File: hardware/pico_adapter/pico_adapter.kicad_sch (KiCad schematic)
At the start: 43 parts, among them J1 L77HDE15SD1CH4F, J2 AudioJack3, J3 5V in, Q1 Q_NMOS_DGS, Q2 Q_NMOS_DGS

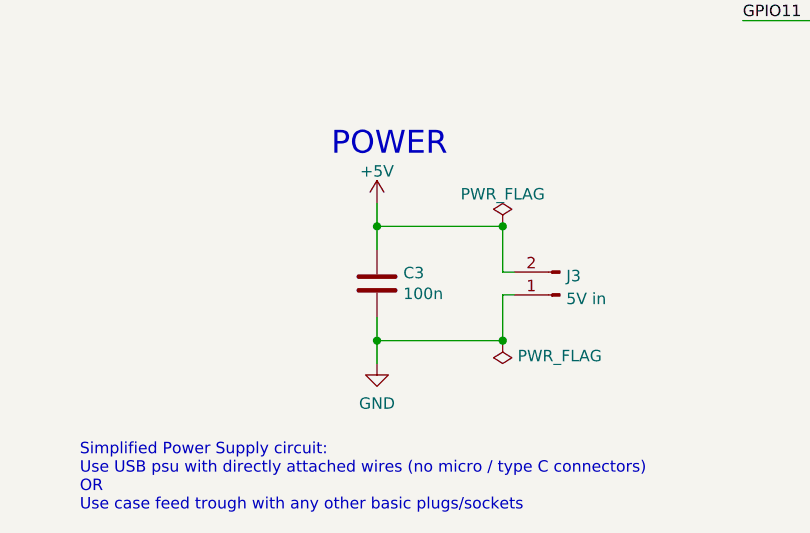
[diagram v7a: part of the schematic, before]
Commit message: UPDATED PICO FOOTPRINT [!] + smaller board
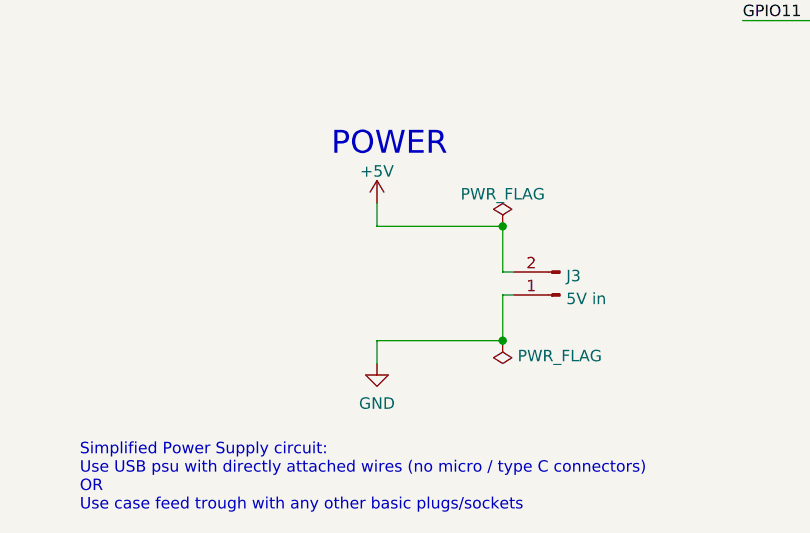
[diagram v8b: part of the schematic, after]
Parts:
- removed C3: 100n, Capacitor_THT:C_Rect_L7.5mm_W6.5mm_P5.00mm, symbol Device:C
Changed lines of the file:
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@@
   (junction (at 137.16 35.56) (diameter 0) (color 0 0 0 0)
   )
-  (junction (at 66.04 138.43) (diameter 0) (color 0 0 0 0)
-  )
   (junction (at 137.16 30.48) (diameter 0) (color 0 0 0 0)
   )
   (junction (at 123.19 62.23) (diameter 0) (color 0 0 0 0)
-  )
-  (junction (at 66.04 151.13) (diameter 0) (color 0 0 0 0)
   )
   (junction (at 220.98 40.64) (diameter 0) (color 0 0 0 0)
@@
     (stroke (width 0) (type default) (color 0 0 0 0))
   )
-  (wire (pts (xy 66.04 138.43) (xy 66.04 140.97))
-    (stroke (width 0) (type default) (color 0 0 0 0))
-  )
   (wire (pts (xy 123.19 25.4) (xy 127 25.4))
     (stroke (width 0) (type default) (color 0 0 0 0))
@@
   )
   (wire (pts (xy 26.67 46.99) (xy 43.18 46.99))
-    (stroke (width 0) (type default) (color 0 0 0 0))
-  )
-  (wire (pts (xy 66.04 148.59) (xy 66.04 151.13))
     (stroke (width 0) (type default) (color 0 0 0 0))
   )
@@
     (pin "9")
   )
-  (symbol (lib_id "Device:C") (at 66.04 144.78 0) (unit 1)
-    (in_bom yes) (on_board yes)
-    (property "Reference" "C3" (id 0) (at 68.961 143.6116 0)
-      (effects (font (size 1.27 1.27)) (justify left))
-    )
-    (property "Value" "100n" (id 1) (at 68.961 145.923 0)
-      (effects (font (size 1.27 1.27)) (justify left))
-    )
-    (property "Footprint" "Capacitor_THT:C_Rect_L7.5mm_W6.5mm_P5.00mm" (id 2) (at 67.0052 148.59 0)
-      (effects (font (size 1.27 1.27)) hide)
-    )
-    (property "Datasheet" "~" (id 3) (at 66.04 144.78 0)
-      (effects (font (size 1.27 1.27)) hide)
-    )
-    (pin "1")
-    (pin "2")
-  )
   (symbol (lib_id "power:PWR_FLAG") (at 80.01 138.43 0) (unit 1)
     (in_bom yes) (on_board yes) (fields_autoplaced)
@@
       (reference "C2") (unit 1) (value "100n") (footprint "Capacitor_THT:C_Rect_L7.5mm_W6.5mm_P5.00mm")
     )
-    (path "/0f4acae6-1474-4661-9a34-e961377aaac1"
-      (reference "C3") (unit 1) (value "100n") (footprint "Capacitor_THT:C_Rect_L7.5mm_W6.5mm_P5.00mm")
-    )
     (path "/80d9d717-f275-4ce8-96c8-5105a1bced0d"
